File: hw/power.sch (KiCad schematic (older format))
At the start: 41 parts, among them J2 USB B Micro, Q1 AP2301, Q2 Si2302CDS, Q3 AP2301, Q8 AP2301, SW1 ON/OFF, U2 AP3401KTTR, U3 MIC2250-2YD5-TR, U4 MCP73831-2ATI, U7 SE809

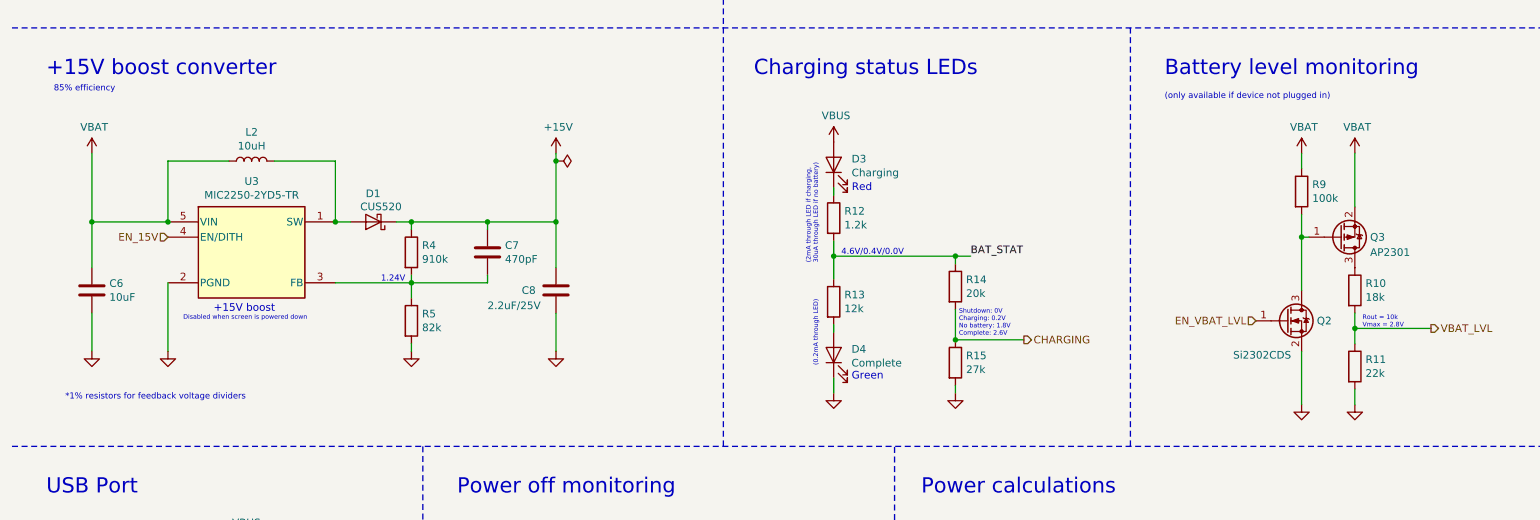
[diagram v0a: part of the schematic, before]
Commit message: Add missing pull down on buzzer H-bridge, 15V enable
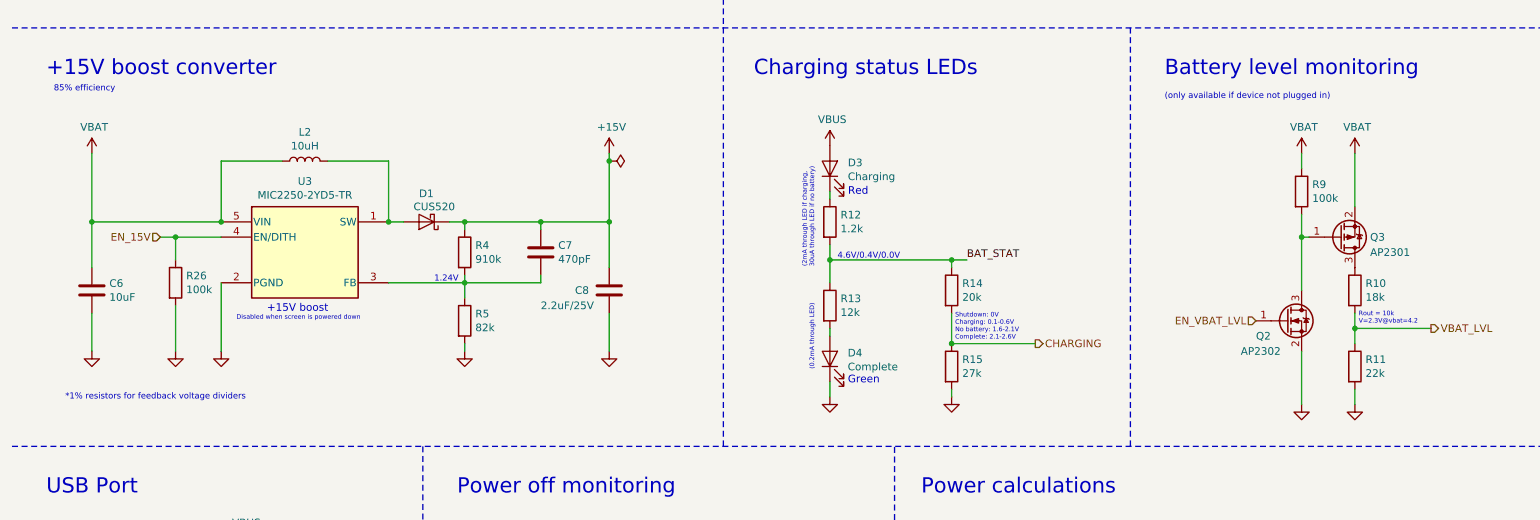
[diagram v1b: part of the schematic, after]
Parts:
- added R26: 100k, Resistor_SMD:R_0603_1608Metric, symbol Device:R
- Q2: value Si2302CDS -> AP2302
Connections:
- net EN_15V: now also R26.1
- net GND: now also R26.2
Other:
- note added: "Rout = 10k\nV=2.3V@vbat=4.2\n"
- note added: "Shutdown: 0V\nCharging: 0.1-0.6V\nNo battery: 1.6-2.1V\nComplete: 2.1-2.6V"
- note removed: "Rout = 10k\nVmax = 2.8V"
- note removed: "Shutdown: 0V\nCharging: 0.2V\nNo battery: 1.8V\nComplete: 2.6V"
- moved on the sheet: C7, C8, D1, D3, D4, L2, R12, R13, R14, R15, R4, R5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
